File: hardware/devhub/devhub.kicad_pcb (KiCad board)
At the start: 4 copper layers, 172.5 x 85 mm, 216 parts, among them J1 USB-C PWR IN, J101 USB-C, J2 USB-C UPSTREAM, J201 USB-C, J3 PORTA 7 (scorta), J301 USB-C, J4 SWD, J401 USB-C, J5 Banana COM 1, J501 USB-A, J6 Banana NC 1, J7 Banana COM 2, J8 Banana NC 2, J9 UART debug, K1 G5Q-1 DC5, K2 G5Q-1 DC5, Q101 AO3400A, Q201 AO3400A, Q301 AO3400A, Q401 AO3400A, Q501 AO3400A, SW1 relè on/off, SW101 porta on/off, SW2 relè on/off, SW201 porta on/off, SW301 porta on/off, SW401 porta on/off, SW501 porta on/off, U1 AP7361C-33E, U101 PI3USB4002A, U12 MCP120T-300I/TT, U13 TPS259470ARPWR, U2 USB2517I-JZX, U201 PI3USB4002A, U3 STM32G0B1RET6, U301 PI3USB4002A, U4 TPS2561ADRC, U401 PI3USB4002A, U5 TPS2561ADRC, U501 PI3USB4002A, U6 TPS2561ADRC, U7 INA3221, U8 INA3221, U9 ULN2003V12, Y1 24MHz 12pF

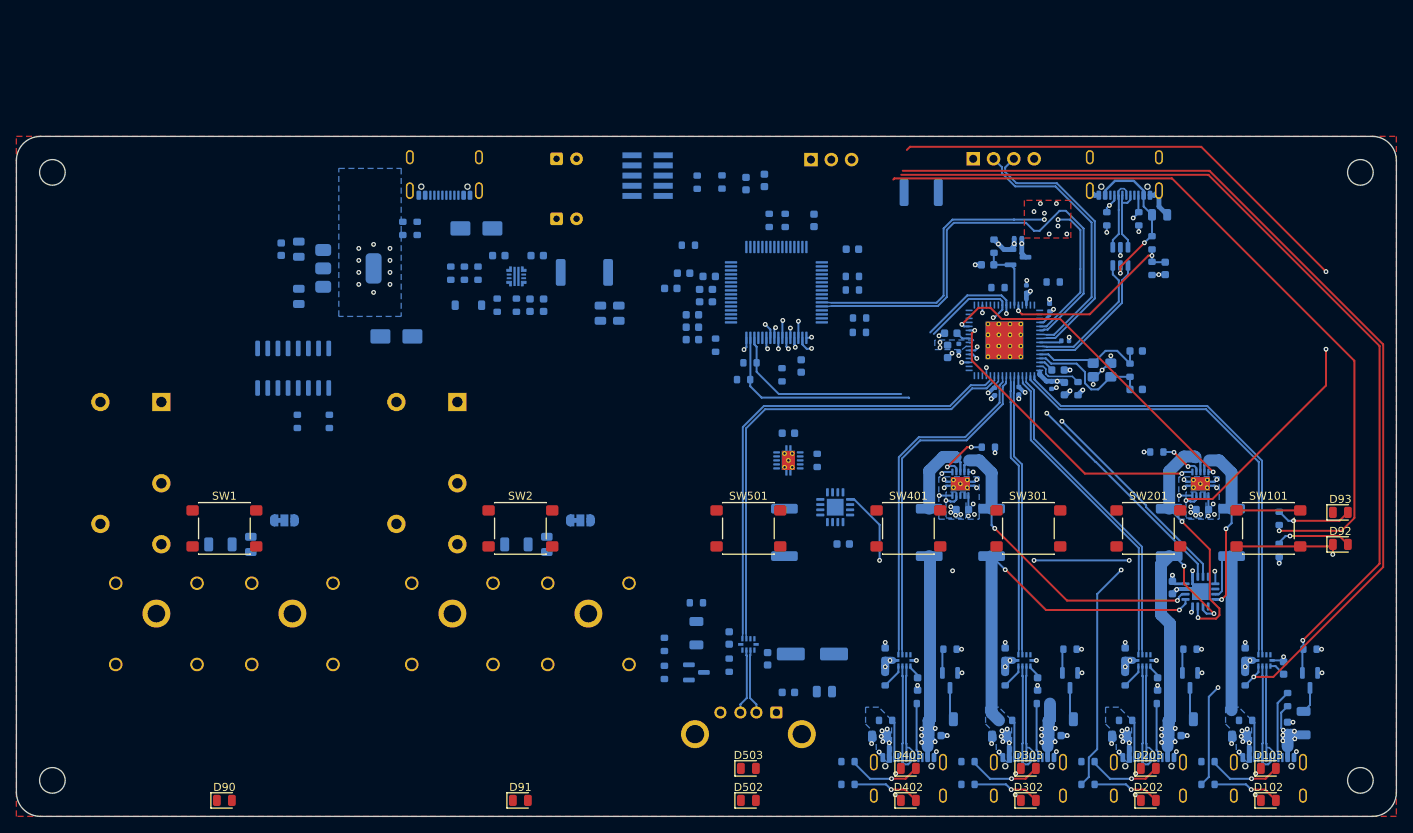
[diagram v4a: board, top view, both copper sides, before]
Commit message: PCB: 100x100 mm outline and initial placement (D84)
- 100x100 mm R3 outline; front: banana jacks at u=10/27, USB-C at
  u=46/61/76/91 (15 mm pitch); M3 holes moved off the front corners
- remove obsolete v0.2 footprints, all tracks, TPS2561A zones,
  second relay keepout and the In1 +3V3 plane; GND_In2 resized
- move functional groups rigidly with their rule areas; place the
  UCS2114 support parts, R50/R51 and the host LED
- UCS2114 footprint: 3 thermal vias 0.6/0.3 mm (annular ring >= 0.15)
- DRC rules: new hub sheet net name, single relay channel
- update PCB rules, hardware README, architecture and decisions
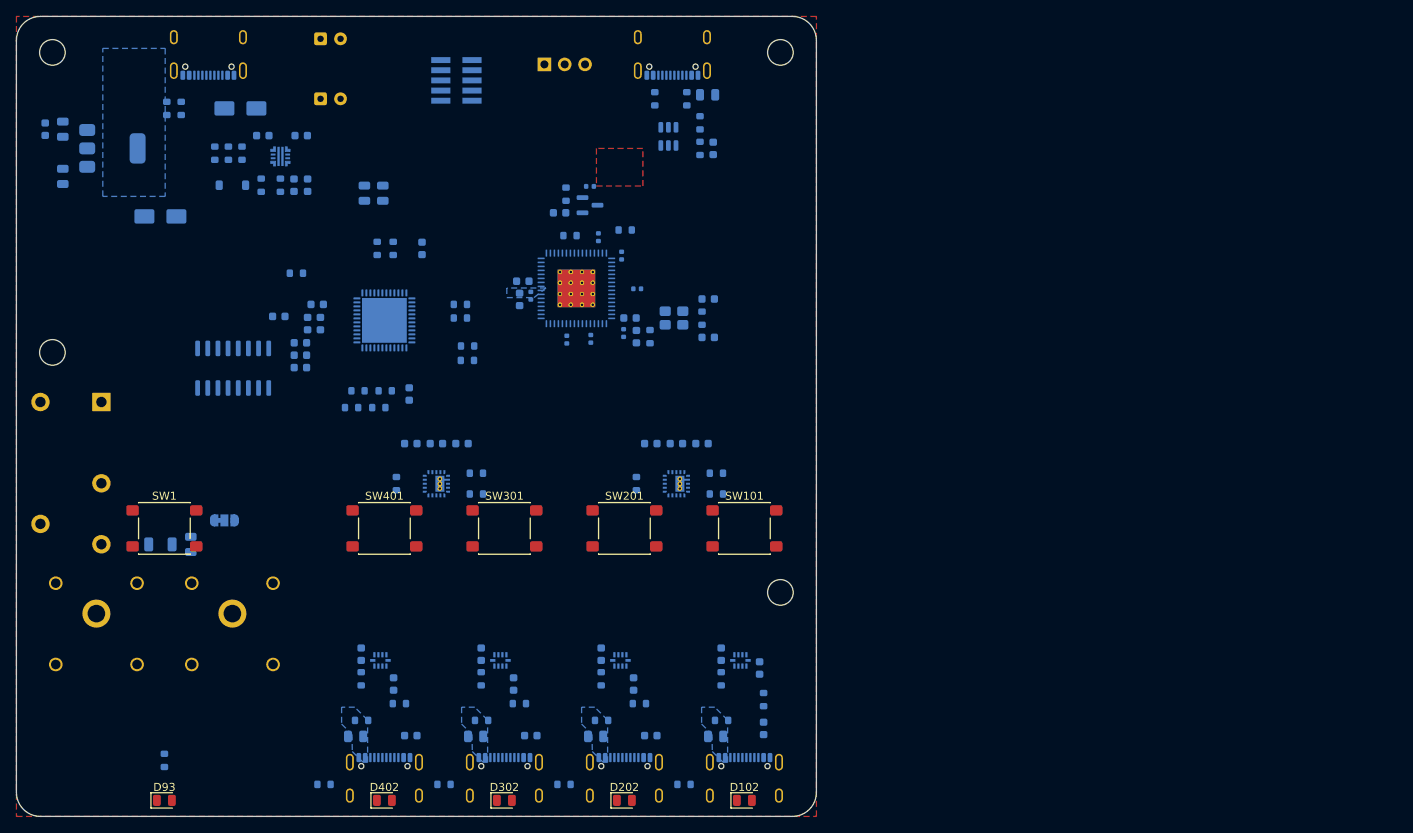
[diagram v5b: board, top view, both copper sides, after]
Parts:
- removed C1, C2, C501, C503, C504, C84: 100n, Capacitor_SMD:C_0603_1608Metric
- removed C502: 22u 10V, Capacitor_SMD:C_0805_2012Metric
- removed C505: 100u 10V, Capacitor_SMD:CP_Elec_6.3x5.8
- removed C506: 1u 25V, Capacitor_SMD:C_0603_1608Metric
- removed C82: 100n 50V DNP, Capacitor_SMD:C_0805_2012Metric
- removed D103, D203, D303, D403, D503: rosso, LED_SMD:LED_0805_2012Metric
- removed D502, D90, D91, D92: verde, LED_SMD:LED_0805_2012Metric
- removed F1: 500mA, Fuse:Fuse_1812_4532Metric
- removed J3: PORTA 7 (scorta), Connector_PinHeader_2.54mm:PinHeader_1x04_P2.54mm_Vertical
- removed J501: USB-A, Connector_USB:USB_A_Kycon_KUSBX-AS1N-B_Horizontal
- removed J7: Banana COM 2, Connector:Banana_Cliff_FCR7350B_S16N-PC_Horizontal
- removed J8: Banana NC 2, Connector:Banana_Cliff_FCR7350R_S16N-PC_Horizontal
- removed JP3: NC/NO, Jumper:SolderJumper-3_P1.3mm_Bridged12_RoundedPad1.0x1.5mm
- removed K2: G5Q-1 DC5, Relay_THT:Relay_SPDT_Omron-G5Q-1
- removed Q101, Q201, Q301, Q401, Q501: AO3400A, Package_TO_SOT_SMD:SOT-23
- removed R101, R201, R301, R401, R501: 100 1206, Resistor_SMD:R_1206_3216Metric
- removed R105, R205, R305, R405, R46, R504, R505: 100k, Resistor_SMD:R_0603_1608Metric
- removed R107, R207, R3, R307, R4, R407, R506, R507, R90, R91, R92: 1k, Resistor_SMD:R_0603_1608Metric
- removed R47: 10k, Resistor_SMD:R_0603_1608Metric
- removed R5, R66, R67, R68, R69: 20m 1% 2512, Resistor_SMD:R_2512_6332Metric
- removed R82: 100 DNP, Resistor_SMD:R_1206_3216Metric
- removed SW2: relè on/off, Button_Switch_SMD:SW_SPST_PTS645Sx43SMTR92
- removed SW501: porta on/off, Button_Switch_SMD:SW_SPST_PTS645Sx43SMTR92
- removed U501: PI3USB4002A, lcsc_footprints:C3657361_UQFN-10_L2_0-W1_5-P0_50-TL
- removed U6: TPS2561ADRC, Package_SON:VSON-10-1EP_3x3mm_P0.5mm_EP1.65x2.4mm_ThermalVias
- removed U7, U8: INA3221, Package_DFN_QFN:Texas_RGV0016A_VQFN-16-1EP_4x4mm_P0.65mm_EP2.1x2.1mm
- added C65: 1u 25V, Capacitor_SMD:C_0603_1608Metric, B.Cu at (116.2, 100.9)
- added R50: 4.7k, Resistor_SMD:R_0603_1608Metric, B.Cu at (106.6, 94.3)
- added R51: 4.7k, Resistor_SMD:R_0603_1608Metric, B.Cu at (105.8, 96.4)
- added R63: 10k, Resistor_SMD:R_0603_1608Metric, B.Cu at (148.0, 104.6)
- added R64: 10k, Resistor_SMD:R_0603_1608Metric, B.Cu at (118.0, 107.2)
- C61, C62, C64: value 100n -> 1u 25V
- R42, R43, R44, R45: value 100k -> 10k
- R60, R61: value 24.3k 1% -> 27k 1%
- R62: value 33.2k 1% -> 10k
- R65: value 20m 1% 2512 -> 10k; footprint Resistor_SMD:R_2512_6332Metric -> Resistor_SMD:R_0603_1608Metric
- U3: value STM32G0B1RET6 -> STM32G0B1CEU6; footprint Package_QFP:LQFP-64_10x10mm_P0.5mm -> Package_DFN_QFN:QFN-48-1EP_7x7mm_P0.5mm_EP5.6x5.6mm
- U4, U5: value TPS2561ADRC -> UCS2114-1-V/LX; footprint Package_SON:VSON-10-1EP_3x3mm_P0.5mm_EP1.65x2.4mm_ThermalVias -> lcsc_footprints:UCS2114_VQFN-20_3x3mm_P0.5mm
- moved D93 151.3 mm to (79.0, 145.5)
- moved R93 142.6 mm to (79.0, 140.5)
- moved C63 96.9 mm to (109.8, 100.9), turned to 0 degrees
- moved R65 94.7 mm to (118.0, 104.6), turned to 0 degrees
- moved H2 76.2 mm to (156.0, 119.5)
- moved R61 74.1 mm to (108.0, 105.9), turned to 90 degrees
- moved H4 74.0 mm to (156.0, 52.0)
- moved C60 69.4 mm to (139.8, 100.9)
- moved C303 65.5 mm to (124.8, 137.4)
- moved C403 65.5 mm to (109.8, 137.4)
- moved C101 65.5 mm to (148.6, 127.2)
- moved C102 65.5 mm to (147.9, 137.5)
- moved C103 65.5 mm to (153.9, 136.5)
- moved C106 65.5 mm to (153.4, 128.9)
- moved C201 65.5 mm to (133.6, 127.2)
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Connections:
- net /Hub USB2517/CC1_UP renamed /Hub USB e switch VBUS/CC1_UP
- net /Hub USB2517/CC2_UP renamed /Hub USB e switch VBUS/CC2_UP
- net /Hub USB2517/HUB_HS_IND renamed /Hub USB e switch VBUS/HUB_HS_IND
- net /Hub USB2517/LOCAL_PWR renamed /Hub USB e switch VBUS/LOCAL_PWR
- net /Hub USB2517/RBIAS renamed /Hub USB e switch VBUS/RBIAS
- net /Hub USB2517/UP_CONN_DN renamed /Hub USB e switch VBUS/UP_CONN_DN
- net /Hub USB2517/UP_CONN_DP renamed /Hub USB e switch VBUS/UP_CONN_DP
- net /Hub USB2517/USBUP_DN renamed /Hub USB e switch VBUS/USBUP_DN
- net /Hub USB2517/USBUP_DP renamed /Hub USB e switch VBUS/USBUP_DP
- net /Hub USB2517/VBUS_UP renamed /Hub USB e switch VBUS/VBUS_UP
- net /Hub USB2517/VDD18 renamed /Hub USB e switch VBUS/VDD18
- net /Hub USB2517/VDD18PLL renamed /Hub USB e switch VBUS/VDD18PLL
- net /Hub USB2517/XTAL1 renamed /Hub USB e switch VBUS/XTAL1
- net /Hub USB2517/XTAL2 renamed /Hub USB e switch VBUS/XTAL2
- net /LED di stato/LED_HOST_K renamed /MCU STM32G0B1/LED_HOST_K
- net /Relè ausiliari/BAN1_2 renamed /Relè ausiliario/BAN1_2
- net /Relè ausiliari/BAN1_COM renamed /Relè ausiliario/BAN1_COM
- net /Relè ausiliari/K1_NC renamed /Relè ausiliario/K1_NC
- net /Relè ausiliari/K1_NO renamed /Relè ausiliario/K1_NO
- net /Relè ausiliari/RLY1_COIL renamed /Relè ausiliario/RLY1_COIL
- net /Relè ausiliari/SNUB1 renamed /Relè ausiliario/SNUB1
- C63 pad 1: +3V3 -> +5V
- C64 pad 1: +3V3 -> +5V
- C7 pad 1: 5V_EFUSE -> +5V
- R106 pad 1: EN_P1 -> LED_P1
- R206 pad 1: EN_P2 -> LED_P2
- R306 pad 1: EN_P3 -> LED_P3
- R40 pad 2: SCL -> I2C1_SCL
- R406 pad 1: EN_P4 -> LED_P4
- R41 pad 2: SDA -> I2C1_SDA
- R60 pad 1: /Load switch e misura corrente/ILIM_U4 -> /Hub USB e switch VBUS/ILIM_U4
- R61 pad 1: /Load switch e misura corrente/ILIM_U5 -> /Hub USB e switch VBUS/ILIM_U5
- R62 pad 1: /Load switch e misura corrente/ILIM_U6 -> +3V3
- R62 pad 2: GND -> FAULT_P1
- R65 pad 1: VBUS_P1 -> +3V3
- R65 pad 2: /Load switch e misura corrente/SW_OUT_P1 -> FAULT_P4
- R93 pad 1: LED_HOST -> /MCU STM32G0B1/LED_HOST
- U13 pad 6: 5V_EFUSE -> +5V
- U2 pad 11: HUB_DN5 -> unconnected-(U2-USBDN5_DM-Pad11)
- U2 pad 12: HUB_DP5 -> unconnected-(U2-USBDN5_DP-Pad12)
- U2 pad 35: FAULT_P5 -> unconnected-(U2-OCS5_N-Pad35)
- U2 pad 40: SDA -> I2C1_SDA
- U2 pad 41: SCL -> I2C1_SCL
- U2 pad 55: /Hub USB2517/SPARE_DN -> unconnected-(U2-USBDN7_DM-Pad55)
- U2 pad 56: /Hub USB2517/SPARE_DP -> unconnected-(U2-USBDN7_DP-Pad56)
- U3 pad 1: FAULT_P3 -> BTN_P1
- U3 pad 10: BTN_P5 -> /MCU STM32G0B1/NRST
- U3 pad 11: HUB_RST_N -> EN_P1
- U3 pad 12: /MCU STM32G0B1/NRST -> EN_P2
- U3 pad 13: EN_P1 -> /MCU STM32G0B1/UART_TX
- U3 pad 14: OE_N_P1 -> /MCU STM32G0B1/UART_RX
- U3 pad 15: DIS_P1 -> FAULT_P4
- U3 pad 16: FAULT_P1 -> LED_P1
- U3 pad 17: CC1_ADC -> unconnected-(U3-PA6-Pad17)
- U3 pad 18: CC2_ADC -> LED_P2
- U3 pad 19: /MCU STM32G0B1/UART_TX -> FAULT_P1
- U3 pad 2: INA_ALERT -> BTN_P2
- U3 pad 20: /MCU STM32G0B1/UART_RX -> EFUSE_FLT_N
- U3 pad 21: RLY1 -> VBUS_DET
- U3 pad 22: RLY2 -> I2C2_SCL
- U3 pad 23: unconnected-(U3-PA6-Pad23) -> I2C2_SDA
- U3 pad 24: EN_P4 -> BTN_P4
- U3 pad 25: EN_P2 -> BTN_RLY1
- U3 pad 26: OE_N_P2 -> OE_N_P3
- U3 pad 27: unconnected-(U3-PB0-Pad27) -> LED_P3
- U3 pad 28: EFUSE_FLT_N -> LED_P4
- U3 pad 29: VBUS_DET -> /MCU STM32G0B1/UCPD1_DBCC1
- U3 pad 3: BTN_P1 -> BTN_P3
- U3 pad 30: unconnected-(U3-PB10-Pad30) -> EN_P3
- U3 pad 31: unconnected-(U3-PB11-Pad31) -> EN_P4
- U3 pad 32: BTN_RLY1 -> /MCU STM32G0B1/UCPD1_DBCC2
- U3 pad 33: BTN_RLY2 -> USB_MCU_DN
- U3 pad 34: unconnected-(U3-PB14-Pad34) -> USB_MCU_DP
- U3 pad 35: LED_FLT_P5 -> /MCU STM32G0B1/SWDIO
- U3 pad 36: LED_HOST -> /MCU STM32G0B1/SWCLK
- U3 pad 37: /MCU STM32G0B1/UCPD1_DBCC1 -> HUB_CFG_SEL2
- U3 pad 38: DIS_P2 -> unconnected-(U3-PD0-Pad38)
- U3 pad 39: FAULT_P2 -> OE_N_P4
- U3 pad 4: BTN_P2 -> +3V3
- U3 pad 40: DIS_P5 -> RLY1
- U3 pad 41: FAULT_P5 -> FAULT_P2
- U3 pad 42: /MCU STM32G0B1/UCPD1_DBCC2 -> OE_N_P1
- U3 pad 43: USB_MCU_DN -> OE_N_P2
- U3 pad 44: USB_MCU_DP -> FAULT_P3
- U3 pad 45: /MCU STM32G0B1/SWDIO -> unconnected-(U3-PB6-Pad45)
- U3 pad 46: /MCU STM32G0B1/SWCLK -> unconnected-(U3-PB7-Pad46)
- U3 pad 47: HUB_CFG_SEL2 -> I2C1_SCL
- U3 pad 48: EN_P3 -> I2C1_SDA
- U3 pad 49: OE_N_P3 -> GND
- U3 pad 5: BTN_P3 -> +3V3
- U3 pad 7: +3V3 -> GND
- U3 pad 8: +3V3 -> /MCU STM32G0B1/LED_HOST
- U3 pad 9: GND -> HUB_RST_N
- U4 pad 1: GND -> EN_P1
- U4 pad 10: FAULT_P1 -> +5V
- U4 pad 11: GND -> VBUS_P2
- U4 pad 2: +5V -> GND
- U4 pad 3: +5V -> /Hub USB e switch VBUS/ILIM_U4
- U4 pad 4: EN_P1 -> VBUS_P1
- U4 pad 5: EN_P2 -> VBUS_P1
- U4 pad 6: FAULT_P2 -> +5V
- U4 pad 7: /Load switch e misura corrente/ILIM_U4 -> +5V
- U4 pad 8: /Load switch e misura corrente/SW_OUT_P2 -> +5V
- U4 pad 9: /Load switch e misura corrente/SW_OUT_P1 -> +5V
- U5 pad 1: GND -> EN_P3
- U5 pad 10: FAULT_P3 -> +5V
- U5 pad 11: GND -> VBUS_P4
- U5 pad 2: +5V -> GND
- U5 pad 3: +5V -> /Hub USB e switch VBUS/ILIM_U5
- U5 pad 4: EN_P3 -> VBUS_P3
- U5 pad 5: EN_P4 -> VBUS_P3
- U5 pad 6: FAULT_P4 -> +5V
- U5 pad 7: /Load switch e misura corrente/ILIM_U5 -> +5V
- U5 pad 8: /Load switch e misura corrente/SW_OUT_P4 -> +5V
- U5 pad 9: /Load switch e misura corrente/SW_OUT_P3 -> +5V
- U9 pad 11: /Relè ausiliari/RLY2_COIL -> unconnected-(U9-O6-Pad11)
- U9 pad 12: /Relè ausiliari/RLY2_COIL -> unconnected-(U9-O5-Pad12)
- U9 pad 13: /Relè ausiliari/RLY2_COIL -> unconnected-(U9-O4-Pad13)
- U9 pad 4: RLY2 -> GND
- U9 pad 5: RLY2 -> GND
- U9 pad 6: RLY2 -> GND
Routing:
- net EN_P1: track 137.5 -> 0.00 mm, vias 4 -> 0
- net OE_N_P1: track 121.8 -> 0.00 mm, vias 1 -> 0
- net DIS_P1: track 113.6 -> 0.00 mm, vias 1 -> 0
- net LED_HOST: track 97.6 -> 0.00 mm, vias 1 -> 0
- net GND: track 92.5 -> 0.00 mm, vias 102 -> 0
- net SDA: track 84.5 -> 0.00 mm, vias 2 -> 0
- net SCL: track 79.8 -> 0.00 mm, vias 2 -> 0
- net VBUS_P3: track 63.2 -> 0.00 mm, vias 12 -> 0
- net HUB_DN5: track 60.3 -> 0.00 mm
- net HUB_DP5: track 60.2 -> 0.00 mm
- net USB_MCU_DP: track 59.1 -> 0.00 mm
- net HUB_DN1: track 57.6 -> 0.00 mm
- net HUB_DP1: track 57.4 -> 0.00 mm
- net USB_MCU_DN: track 56.0 -> 0.00 mm, vias 2 -> 0
- net INA_ALERT: track 53.9 -> 0.00 mm, vias 4 -> 0
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- removed copper zone on In1.Cu, net +3V3
- removed copper zone on B.Cu, net +5V
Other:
- board size 172.5 x 85 mm -> 100 x 100 mm
- board text added: "FRONTE (lato banco): boccole COM/NC, porte USB-C 4-3-2-1"
- board text added: "RETRO: alimentazione J1, upstream J2"
- board text added: "Vista dall'alto. Faccia superiore (F): LED e pulsanti; faccia inferiore (B): tutto il resto"
- board text removed: "Alimentazione"
- board text removed: "FRONTE (lato banco): porte 1-5, boccole relè"
- board text removed: "Faccia superiore (F): LED e pulsanti; faccia inferiore (B): tutto il resto"
- board text removed: "Hub USB2517"
- board text removed: "LED di stato"
- board text removed: "Load switch e misura corrente"
- board text removed: "MCU STM32G0B1"
- board text removed: "Porta 1 (USB-C)"
- board text removed: "Porta 2 (USB-C)"
- board text removed: "Porta 3 (USB-C)"
- board text removed: "Porta 4 (USB-C)"
- board text removed: "Porta 5 (USB-A)"
- board text removed: "RETRO: alimentazione e upstream"
- board text removed: "Relè ausiliari"

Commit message: PCB: reuse v0.2 routing where relative placement is unchanged
- import v0.2 tracks and vias per functional group with the same
  translation (ports, hub, upstream, power), renaming changed nets
- drop items whose pads changed net (EN to LED resistors), old
  TPS2561A-area routing, USB_MCU fragments and stray stubs
- remove the stale F.Cu GND zone, restrict GND_In2 to In2.Cu, restore
  the In1 +3V3 plane and the VBUS islands used by the imported vias
- update PCB notes in hardware/README.md and regole-pcb.md
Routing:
- net GND: track 0.00 -> 60.2 mm, vias 0 -> 72
- net +3V3: track 0.00 -> 32.8 mm, vias 0 -> 17
- net VBUS_P2: track 0.00 -> 26.0 mm, vias 0 -> 10
- net I2C1_SDA: track 0.00 -> 25.5 mm, vias 0 -> 1
- net VBUS_DET: track 0.00 -> 21.8 mm, vias 0 -> 1
- net I2C1_SCL: track 0.00 -> 18.4 mm, vias 0 -> 1
- net VBUS_P1: track 0.00 -> 17.0 mm, vias 0 -> 10
- net /Hub USB e switch VBUS/XTAL1: track 0.00 -> 15.9 mm
- net VBUS_P3: track 0.00 -> 15.7 mm, vias 0 -> 10
- net /Hub USB e switch VBUS/USBUP_DP: track 0.00 -> 15.1 mm
- net FAULT_P1: track 0.00 -> 14.7 mm, vias 0 -> 1
- net /Hub USB e switch VBUS/XTAL2: track 0.00 -> 14.6 mm
- net /Hub USB e switch VBUS/USBUP_DN: track 0.00 -> 14.4 mm
- net VBUS_P4: track 0.00 -> 14.4 mm, vias 0 -> 10
- net LED_P1: track 0.00 -> 14.3 mm, vias 0 -> 1
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- added copper zone on In1.Cu, net +3V3
- removed copper zone on F.Cu, net GND

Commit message: PCB: make port 1 layout identical to ports 2-4
C103, C106 and R102 moved to the same position relative to J101 as in
the other ports; port 1 local routing replaced with a copy of port 2
shifted by 15 mm (VBUS branch towards the UCS2114 left to route).
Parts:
- moved H1 20.5 mm to (79.7, 103.8)
- moved C106 2.14 mm to (152.7, 130.9), turned to -90 degrees
- moved C103 1.27 mm to (154.8, 137.4), turned to 0 degrees
- moved R102 0.73 mm to (153.4, 133.4), turned to 180 degrees
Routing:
- net LED_P1: track 14.3 -> 0.00 mm, vias 1 -> 0
- net VBUS_P1: track 17.0 -> 14.4 mm
- net OE_N_P1: track 5.56 -> 3.10 mm, vias 1 -> 0
- net /Porta 1 (USB-C)/CC1: track 8.63 -> 6.85 mm
- net VBUS_P2: track 26.0 -> 24.4 mm
- net GND: track 60.2 -> 60.6 mm, vias 72 -> 75

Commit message: Power stage: lower eFuse OVLO, SMD bulk caps, move button row (D85-D87)
- R30/R31 68.1k/8.66k: OVLO 5.52-5.90 V, below the 6 V abs max of UCS2114
- C3/C4 Panasonic EEE-FK1C221XP SMD 220 uF 16 V replace THT radials
- Buttons at v = 14.5 mm from the front edge
- Update power budget and LDO dissipation for four ports
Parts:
- C3, C4: value 220u 10V -> 220u 16V; footprint Capacitor_THT:CP_Radial_D6.3mm_P2.50mm -> Capacitor_SMD:CP_Elec_6.3x7.7
- R30: value 69.8k 1% -> 68.1k 1%
- R31: value 9.53k 1% -> 8.66k 1%
- moved SW1 21.5 mm to (79.0, 133.0)
- moved SW101 21.5 mm to (151.5, 133.0)
- moved SW201 21.5 mm to (136.5, 133.0)
- moved SW301 21.5 mm to (121.5, 133.0)
- moved SW401 21.5 mm to (106.5, 133.0)
- moved C60 10.5 mm to (139.8, 111.4)
- moved C61 10.5 mm to (143.0, 111.4)
- moved C62 10.5 mm to (146.2, 111.4)
- moved C63 10.5 mm to (109.8, 111.4)
- moved C64 10.5 mm to (113.0, 111.4)
- moved C65 10.5 mm to (116.2, 111.4)
- moved R60 10.5 mm to (138.0, 116.4)
- moved R61 10.5 mm to (108.0, 116.4)
- moved R62 10.5 mm to (148.0, 117.7)
- moved R63 10.5 mm to (148.0, 115.1)
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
